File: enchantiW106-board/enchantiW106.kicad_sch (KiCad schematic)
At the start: 73 parts, among them J1 USB_C_Receptacle_USB2.0, J3 Programming Header, SW1 B3U-1000P, SW2 B3U-1000P, U1 USBLC6-2P6, U11 MAX17262REWL+T, U12 BQ25185DLHR, U13 ICM-42670-P, U2 MMC5633NJL, U3 IRIS-W106-00B, U4 NCP167AMX330TBG, U5 STM32H523CET6, U9 NCP167AMX330TBG

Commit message: removed stm32 co-processor for simplicity, switched to 1.8V IO, swapped to akm magnetometer
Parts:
- removed BT1: JST-PH-1x02-2.000mm, Connector_JST:JST_PH_S2B-PH-SM4-TB_1x02-1MP_P2.00mm_Horizontal, symbol Connector_Generic_MountingPin:Conn_01x02_MountingPin
- removed C12, C4, C5, C6: 1uF, Capacitor_SMD:C_0402_1005Metric, symbol Device:C
- removed C14, C2: 2.2uF, Capacitor_SMD:C_0402_1005Metric, symbol Device:C
- removed C16, C20, C24, C25, C26: 0.1uF, Capacitor_SMD:C_0402_1005Metric, symbol Device:C
- removed C3: 220nF, Capacitor_SMD:C_0402_1005Metric, symbol Device:C
- removed CHARGLED1: S1, LED_SMD:LED_0402_1005Metric, symbol Device:LED
- removed FP2: CONN HEADER SMD 6POS 1MM, Connector_Molex:Molex_Pico-Clasp_501331-0807_1x08-1MP_P1.00mm_Vertical, symbol ENCHANTI_connectors:PicoClasp_8pin
- removed R12, R13: 2k2, Resistor_SMD:R_0402_1005Metric, symbol Device:R_US
- removed R4, R5, R9: 10k, Resistor_SMD:R_0402_1005Metric, symbol Device:R_US
- removed SW1, SW2: B3U-1000P, Button_Switch_SMD:SW_SPST_B3U-1000P, symbol Switch:SW_Push
- removed SYS6: SYS, symbol power-symbols:VSYS
- removed TOUCH1: JST-SH-1x04 1.0mm, ENCHANTI_connectors:JST_SMD_1.0mm-4_Vertical, symbol ENCHANTI_connectors:QWIIC-CONNECTOR
- removed TP1: TestPoint, TestPoint:TestPoint_Pad_D1.0mm, symbol Connector:TestPoint
- removed U11: MAX17262REWL+T, ENCHANTI_battery-management:MAX17262, symbol ENCHANTI_battery-management:MAX17262REWL+T
- removed U2: MMC5633NJL, Package_BGA:WLP-4_0.86x0.86mm_P0.4mm, symbol Sensor_Magnetic:MMC5633NJL
- removed U4, U9: NCP167AMX330TBG, ENCHANTI_regulators:XDFN4_1X1_711AJ_ONS, symbol ENCHANTI_regulators:NCP167AMX330TBG
- removed U5: STM32H523CET6, ENCHANTI_mcus:LQFP48_STM, symbol ENCHANTI_mcus:STM32H523CET6
- added BAT?: JST_SMD_2.0, ENCHANTI_connectors:Battery_JST_2pin, symbol ENCHANTI_connectors:Battery_JST_2pin
- added C? (x2): 0.1uF, Capacitor_SMD:C_0402_1005Metric, symbol Device:C
- added C? (x3): 1uF, Capacitor_SMD:C_0402_1005Metric, symbol Device:C
- added CHARGLED3: RED_LED, LED_SMD:LED_0603_1608Metric, symbol Device:LED
- added CHARGLED4: YELLOW_LED, LED_SMD:LED_0603_1608Metric, symbol Device:LED
- added FP2: CONN HEADER SMD 6POS 1MM, Connector_Molex:Molex_Pico-Clasp_501331-0607_1x06-1MP_P1.00mm_Vertical, symbol ENCHANTI_connectors:PicoClasp_6pin
- added LED7: Green, LED_SMD:LED_0402_1005Metric, symbol Device:LED
- added QWIIC2: JST-SH-1x04 1.0mm, ENCHANTI_connectors:JST_SMD_1.0mm-4_Vertical, symbol ENCHANTI_connectors:QWIIC-CONNECTOR
- added R75, R76, R77: 2k, Resistor_SMD:R_0402_1005Metric, symbol Device:R_US
- added R78: 36.5k, Resistor_SMD:R_0402_1005Metric, symbol Device:R_US
- added R?: 1mOhm, ENCHANTI_resistors:L4CC0306, symbol ENCHANTI_resistors:L4CC0306RLR001FNR
- added R? (x2): 100k, Resistor_SMD:R_0402_1005Metric, symbol Device:R_US
- added R? (x2): 10k, Resistor_SMD:R_0402_1005Metric, symbol Device:R_US
- added R? (x2): 2k2, Resistor_SMD:R_0402_1005Metric, symbol Device:R_US
- added SW1, SW2, SW3: PTS810, ENCHANTI_switches:SW_SPST_PTS810, symbol ENCHANTI_switches:PTS810
- added SYS3, SYS5, SYS? (x3): SYS, symbol power-symbols:VSYS
- added TP2, TP? (x2): TestPoint, SparkFun-Connector:TestPoint-0.75mm, symbol Connector:TestPoint
- added U7: TPS7A20L33PDQNR, ENCHANTI_regulators:Texas_X2SON-4_1x1mm_P0.65mm, symbol ENCHANTI_regulators:TPS7A20L
- added U?: SN74LVC2G07DCKR, ENCHANTI_logicICs:Texas_DCK6, symbol ENCHANTI_logicICs:SN74LVC2G07DCKR
- added U?: TPS63900, Package_SON:WSON-10-1EP_2.5x2.5mm_P0.5mm_EP1.2x2mm_ThermalVias, symbol Regulator_Switching:TPS63900
- added U?: AK09940A, ENCHANTI_MEMS:LGA11_1p6x1p6x0p58_AKM, symbol ENCHANTI_mems:AK09940A
- added U?: TPS7A20L18PDQNR, ENCHANTI_regulators:Texas_X2SON-4_1x1mm_P0.65mm, symbol ENCHANTI_regulators:TPS7A20L
- added U?: MAX17260SETD+T, ENCHANTI_battery-management:TDFN-14-EP-ADI, symbol ENCHANTI_battery-management:MAX17260SETD+T
- C1: value 1uF -> 22uF; footprint Capacitor_SMD:C_0402_1005Metric -> Capacitor_SMD:C_0603_1608Metric; Manufacturer Samsung Electro-Mechanics -> Murata Electronics; Mfg Part # CL05A105KO5NNNC -> GRM187R61A226ME15; mpn CL05A105KO5NNNC -> CL10A105KO8NNNC
- C10: value 4.7uF -> 1uF; Mfg Part # CL05A475MO5NUNC -> CL05A105KO5NNNC; mpn CL05A105KO5NNNC -> (none)
- C11: mpn CL05A105KO5NNNC -> (none)
- C?: renamed from C18; Manufacturer Samsung Electro-Mechanics -> Murata Electronics; Mfg Part # CL05B104KO5NNNC -> GRM155R71C104KA88J
- C?: renamed from C8; mpn GRT155R61C474KE01D -> (none)
- C?: renamed from C17; Manufacturer Samsung Electro-Mechanics -> Murata Electronics; Mfg Part # CL05A105KO5NNNC -> GRM155R61E105KA12D
- C?: renamed from C7; mpn CL05B104KO5NNNC -> (none)
- R3: value 2k2 -> 100k; Manufacturer Panasonic Electronic Components -> YAGEO; Mfg Part # ERJ-2RKF2201X -> RC0402FR-07100KL; mpn ERJ-2RKF2201X -> ERJ-2RKF1001X
- renumbered U13 to U?
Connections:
- net NRST is gone; now on net +3V3: C1.1
- net SPI2_CIPO is gone; now on net IMU_CIPO: U3.N10 (GPIO[3])
- net SPI2_COPI is gone; now on net IMU_COPI: U3.M10 (GPIO[2])
- net SPI2_CS is gone; now on net IMU_CS: U3.M11 (GPIO[0])
- net SPI2_SCLK is gone; now on net IMU_SCLK: U3.M9 (GPIO[4])
- net +3V3: now also C13.1, C19.1, R3.1, U?.6 (VOUT); no longer C10.1
- net +BATT: now also BAT?.1 (+), R?.1, TP?.1, U?.1 (TH), U?.6 (BATT)
- net 3V3_AUX: now also U3.L6 (VCCIO), U3.L7 (+1V8), FP2.3 (Pin_3); no longer ANG1.1 (Pin_1), ANG3.1 (Pin_1), C13.1, C19.1, C?.1, C?.1, U?.5 (VDDIO), U?.8 (VDD)
- net BOOT: now also SW2.1
- net CHRG+: now also R?.2
- net EN: now also R3.2, SW1.1; no longer J3.10 (RES)
- net GND: now also BAT?.2 (-), BAT?.MP (mp), C?.2, C?.2, C?.2, C?.2, C?.2, FP2.1 (Pin_1), FP2.MP (MountPin), QWIIC2.1 (GND), R77.2, R78.2, SW1.2, SW2.2, U7.2 (GND), U7.5 (Pad), U?.11 (GND), U?.12 (ALRT), U?.15 (EPAD), U?.2 (GND), U?.2 (GND), U?.4 (CFG2), U?.5 (CFG3), U?.5 (Pad), U?.8 (GND), U?.8 (GND), U?.9 (CSPL), U?.C1 (VSS), U?.D1 (CAD0), U?.D2 (CAD1); no longer R3.2, STATLED1.1 (K), STATLED2.1 (K)
- net I2C2_SCL: now also QWIIC2.4 (SCL)
- net I2C2_SDA: now also QWIIC2.3 (SDA)
- net LDO_EN: now also U?.3 (EN)
- net REG: now also U?.11 (REG)
- net STAT1: now also R75.2
- net STAT2: now also R76.2
- net SYS: now also C10.1, STATLED1.2 (A), STATLED2.2 (A), C?.1, CHARGLED3.2 (A), CHARGLED4.2 (A), SYS3.1 (SYS), SYS5.1 (SYS), SYS?.1 (SYS), SYS?.1 (SYS), SYS?.1 (SYS), U7.4 (IN), U?.1 (EN), U?.10 (VIN), U?.2 (SEL), U?.4 (IN); no longer C11.1
- net at R8.2: now also STATLED1.1 (K); no longer STATLED1.2 (A)
- net JTAG_TDO: now reaches U3.A12 (JTAG_TDO)
- net JTAG_TDO: now also J3.6 (SWO)
- net JTAG_TMS: now reaches U3.A14 (JTAG_TMS)
- net JTAG_TMS: now also J3.2 (SWDIO)
- net JTAG_nRST: now reaches U3.B11 (JTAG_nRST)
- net JTAG_nRST: now also J3.10 (RES)
- net JTAG_TDI: now reaches U3.B12 (JTAG_TDI)
- net JTAG_TDI: now also J3.8 (TDI)
- net JTAG_TCK: now reaches U3.B14 (JTAG_TCK)
- net JTAG_TCK: now also J3.4 (SWCLK)
- net at R10.2: now also STATLED2.1 (K); no longer STATLED2.2 (A)
- net at U3.L8 (+3V3): no longer U3.L6 (VCCIO)
- net BLUELED: no longer names the net of R8.1
- net BLUELED: now also U?.4 (2Y); no longer U3.L4 (RMII_INT)
- net LED1: no longer names the net of U3.A2 (QSPI_RCLK)
- net ORANGELED: no longer names the net of R10.1
- net ORANGELED: now also U?.6 (1Y); no longer U3.E2 (GPIO[27])
- net SPI1_CIPO renamed IMU_CIPO
- net SPI1_COPI renamed IMU_COPI
- net SPI1_CS renamed IMU_CS
- net IMU_CS: now also R?.2
- net SPI1_SCLK renamed IMU_SCLK
- net SWDCLK: no longer names the net of U3.A6 (FC2_RxD)
- net SWDCLK: no longer J3.4 (SWCLK)
- net SWDIO: no longer names the net of U3.B5 (FC2_TxD)
- net SWDIO: no longer J3.2 (SWDIO)
- new net: LED7.1 (K), R77.1
- new net: CHARGLED3.1 (K), R75.1
- new net: CHARGLED4.1 (K), R76.1
- new net: QWIIC2.NC1 (NC), QWIIC2.NC2 (NC)
- new net: R78.1, U?.3 (CFG1)
- new net +1V8: C?.1, R?.1, R?.2, U?.5 (VCC)
- new net +1V8_AUX: ANG1.1 (Pin_1), ANG3.1 (Pin_1), C?.1, C?.1, C?.1, C?.1, C?.1, R?.1, R?.1, R?.2, R?.2, TP?.1, U?.1 (OUT), U?.5 (VDDIO), U?.8 (VDD), U?.B1 (VDD), U?.C4 (VIO), U?.D4 (RSTN)
- new net +3V3_AUX: C11.1, FP2.2 (Pin_2), LED7.2 (A), QWIIC2.2 (3v3), TP2.1, U7.1 (OUT)
- new net 3V3_EN: U7.3 (EN)
- new net BLUELED_EN: R?.1, U3.L4 (RMII_INT), U?.1 (1A)
- new net BUTTON: FP2.6 (Pin_6)
- new net CSN: R?.3 (CSN), U?.7 (CSN)
- new net CSPH: R?.4 (CSP), U?.10 (CSPH)
- new net I2C_SCL: FP2.5 (Pin_5), R?.1, U?.14 (SCL)
- new net I2C_SDA: FP2.4 (Pin_4), R?.1, U?.13 (SDA)
- new net MAG_CIPO: U?.B4 (SO)
- new net MAG_COPI: U?.A4 (SDA/SI)
- new net MAG_CS: R?.2, U?.A2 (CSB/SPI_CS)
- new net MAG_INT: U?.A1 (DRDY/TRG)
- new net MAG_SCLK: U?.A3 (SCL/SK)
- new net ORANGELED_EN: R?.2, U3.E2 (GPIO[27]), U?.3 (2A)
- no-connect marks 93 -> 70
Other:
- note added: "1V8 0.3A LDO (IMU + Sensors + ADC)"
- note added: "3.3V - Main Regulator, 1.45A buck-boost converter"
- note added: "3.3V Power Good LED"
- note added: "3V3 0.3A LDO (CAN transceiver + External Boards)"
- note added: "6 axis IMU"
- note added: "9-DOF Motion Sensing"
- note added: "AK09940A Magnetometer"
- note added: "Boot Button (ISP Boot)"
- note added: "Connector for Front plate"
- note added: "ESD Protection for USB input"
- note added: "FSR Connectors"
- note added: "LED For Battery charging status, Table 8.2 in BQ25185 datasheet for outputs"
- note added: "Reset Button"
- note added: "STATUS LEDS"
- note added: "USB C CONNECTOR + ESD Protection"
- note added: "User Button (Wakeup)"
- note added: "User LEDs"
- note added: "pullup for chip select pin"
- note removed: "3.3V - AUX Regulator"
- note removed: "3.3V Regulator"
- note removed: "BLUE LED == Connected to Wifi"
- note removed: "Connect to Frontplate"
- note removed: "FSR CONNECTOR"
- note removed: "Front Connector"
- note removed: "IMU"
- note removed: "ORANGE LED == Setting up/Fail State"
- note removed: "Qwiic connector to connect other I2C devices"
- note removed: "STATUS LED"
- note removed: "STM32H523CE - Sensor Processing Companion"
- note removed: "Test point for current measurement"
- note removed: "USB C CONNECTOR"
- note removed: "VDD Filtering"
- note removed: "VDDA Filtering"
- moved on the sheet: ANG1, ANG3, BOARDLAYOUT1, C15, C21, C22, C23, C9, C?, J1, J3, R1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

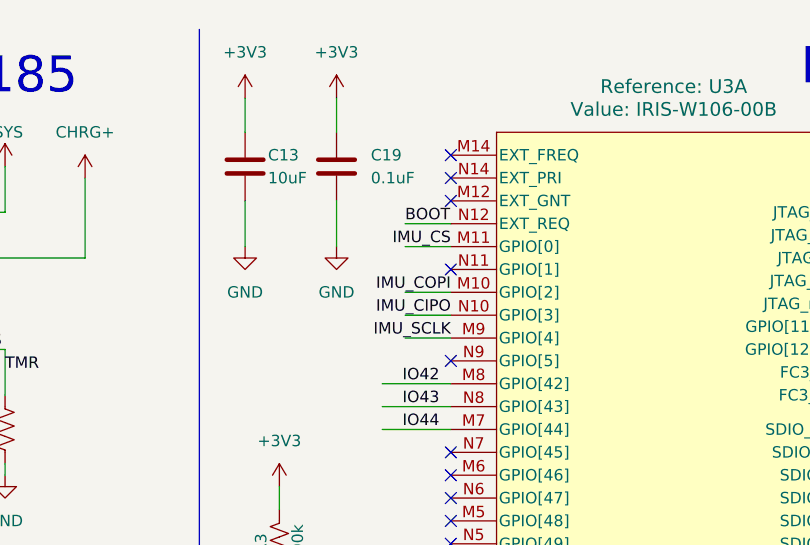
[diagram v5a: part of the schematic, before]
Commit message: added IMU interrupt
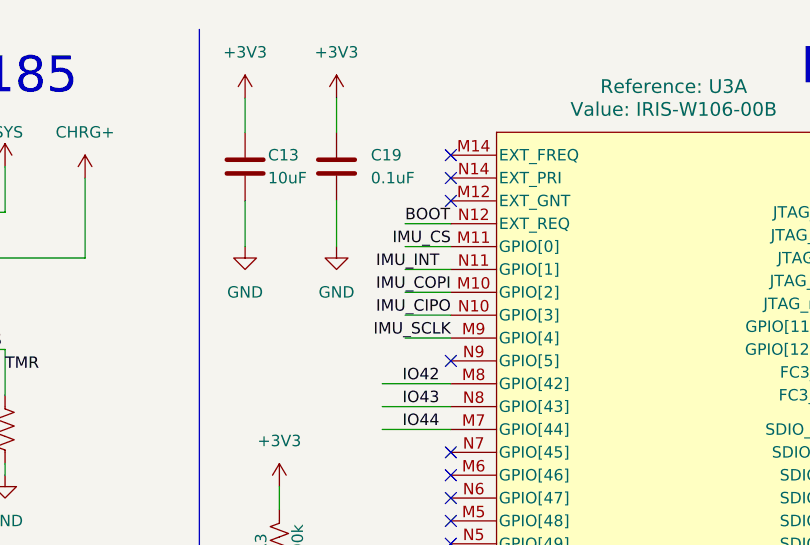
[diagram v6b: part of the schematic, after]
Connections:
- net IMU_INT: now also U3.N11 (GPIO[1])
- no-connect marks 70 -> 69
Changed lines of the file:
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@@
 	)
 	(no_connect
-		(at 138.43 39.37)
-	)
-	(no_connect
 		(at 187.96 72.39)
 	)
@@
 	(wire
 		(pts
+			(xy 133.35 39.37) (xy 138.43 39.37)
+		)
+		(stroke
+			(width 0)
+			(type default)
+		)
+	)
+	(wire
+		(pts
 			(xy 219.71 259.08) (xy 219.71 256.54)
 		)
@@
 		(effects
 			(font
+				(size 1.27 1.27)
+			)
+			(justify right bottom)
+		)
+	)
+	(label "IMU_INT"
+		(at 137.16 39.37 180)
+		(effects
+			(font

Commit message: started routing the pcb
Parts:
- removed R? (x2): 10k, Resistor_SMD:R_0402_1005Metric, symbol Device:R_US
- removed SW3: PTS810, ENCHANTI_switches:SW_SPST_PTS810, symbol ENCHANTI_switches:PTS810
- added L1: 2.2uH, ENCHANTI_inductors:DFE252012P-1R0M=P2, symbol ENCHANTI_inductors:DFE252012F-2R2M
- gave numbers to parts that had none: 26
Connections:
- net +1V8 is gone; now on net +1V8_AUX: C5.1, R12.1, R13.2, U6.5 (VCC)
- net LDO_EN is gone; now on net 1V8_EN: U5.3 (EN)
- net RX is gone; now on net I2C2_SDA: U3.B9 (FC3_RxD)
- net TX is gone; now on net I2C2_SCL: U3.A10 (FC3_TxD)
- net +3V3: now also U3.H1 (VCC), U3.H2 (VCC), U3.H3 (VCC)
- net +3V3_AUX: now also BOARDLAYOUT1.2.1 (3v3)
- net 3V3_EN: now also U3.M4 (GPIO[50])
- net BUTTON: now also U3.F3 (RMII_CLK)
- net FSR1: now also U3.N6 (GPIO[47])
- net FSR2: now also U3.M6 (GPIO[46])
- net I2C_SCL: now also U3.B5 (FC2_TxD)
- net I2C_SDA: now also U3.A6 (FC2_RxD)
- net MAG_CIPO: now also U3.L2 (RMII_MDC)
- net MAG_COPI: now also U3.L1 (RMII_MDIO)
- net MAG_CS: now also U3.N3 (GPIO[53])
- net MAG_INT: now also U3.N4 (GPIO[51])
- net MAG_SCLK: now also U3.N2 (GPIO[54])
- net 1V8_EN: now reaches U3.K1 (RMII_TxD0)
- net at U4.7 (LX2): now also L1.1
- net at U4.9 (LX1): now also L1.2
- net 3V3_AUX renamed VCCIO
- net VCCIO: no longer BOARDLAYOUT1.2.1 (3v3), U3.H1 (VCC), U3.H2 (VCC), U3.H3 (VCC)
- no-connect marks 69 -> 60
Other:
- note removed: "User Button (Wakeup)"
- note removed: "pullup for chip select pin"
- moved on the sheet: C10, C11, C12, C14, C7, C8, QWIIC2, TP2, U7, U8, U9

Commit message: updated schematic with BOM information
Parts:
- R78: Manufacturer Panasonic Electronic Components -> YAGEO; Mfg Part # (none) -> RC0402FR-0736K5L
- U4: Manufacturer (none) -> Texas Instruments; Mfg Part # (none) -> TPS63900DSKR
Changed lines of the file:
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@@
 			)
 		)
-		(property "Description" ""
+		(property "Description" "36.5 kOhms ±1% 0.063W, 1/16W Chip Resistor 0402 (1005 Metric)"
 			(at 161.29 184.15 0)
 			(effects
@@
 			)
 		)
-		(property "Mfg Part #" ""
+		(property "Mfg Part #" "RC0402FR-0736K5L"
 			(at 161.29 184.15 0)
 			(effects
@@
 			)
 		)
-		(property "Manufacturer" "Panasonic Electronic Components"
+		(property "Manufacturer" "YAGEO"
 			(at 161.29 184.15 0)
 			(effects
@@
 			)
 		)
-		(property "Description" "Buck-Boost Converter, 1.8-5.5V Input Voltage, 0.4A Switch Current, Adjustable 1.8-5V Output Voltage, WSON-10"
+		(property "Description" "Buck-Boost Switching Regulator IC Positive Programmable 1.8V 1 Output 400mA 10-WFDFN Exposed Pad"
 			(at 146.05 184.15 0)
 			(effects
+				(font
+					(size 1.27 1.27)
+				)
+				(hide yes)
+			)
+		)
+		(property "Mfg Part #" "TPS63900DSKR"
+			(at 146.05 184.15 0)
+			(effects
+				(font
+					(size 1.27 1.27)
+				)
+				(hide yes)
+			)
+		)
+		(property "Manufacturer" "Texas Instruments"
+			(at 146.05 184.15 0)
+			(effects
